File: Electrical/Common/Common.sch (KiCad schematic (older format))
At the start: 76 parts, among them J201 01x03, J202 01x04, J203 01x03, J204 01x04, J205 01x03, J206 USB_OTG, J207 01x04, J208 01x02, J209 01x04, J210 01x02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

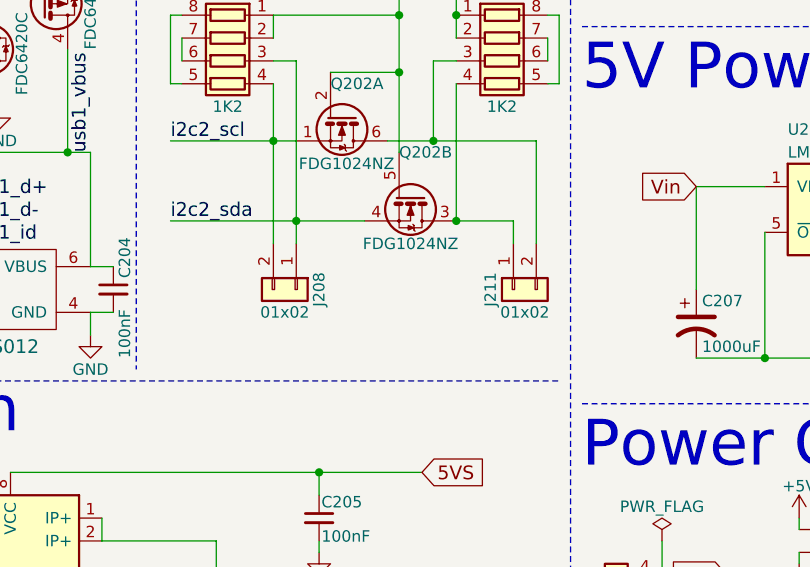
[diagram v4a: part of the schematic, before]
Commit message: Made pin one consistantly SCL on both sets of I2C headers.
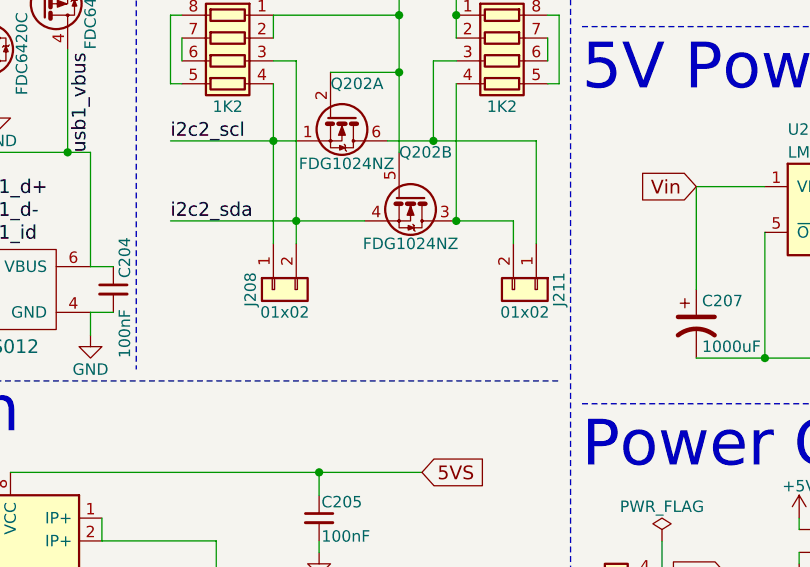
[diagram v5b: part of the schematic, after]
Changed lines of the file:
@@
 LIBS:allegro
 LIBS:mechanical
-LIBS:Dual-cache
+LIBS:Quad-cache
 EELAYER 25 0
 EELAYER END
 $Descr A4 11693 8268
 encoding utf-8
-Sheet 2 4
+Sheet 2 6
 Title ""
 Date ""
@@
 L Conn_01x02 J208
 U 1 1 5A50A269
-P 6200 3250
-F 0 "J208" H 6200 3350 50  0000 C CNN
-F 1 "01x02" V 6300 3200 50  0000 C CNN
-F 2 "Pin_Headers:Pin_Header_Straight_1x02_Pitch2.54mm" H 6200 3250 50  0001 C CNN
-F 3 "" H 6200 3250 50  0001 C CNN
-	1    6200 3250
-	0    1    1    0
+P 6100 3250
+F 0 "J208" H 6100 3350 50  0000 C CNN
+F 1 "01x02" V 6200 3200 50  0000 C CNN
+F 2 "Pin_Headers:Pin_Header_Straight_1x02_Pitch2.54mm" H 6100 3250 50  0001 C CNN
+F 3 "" H 6100 3250 50  0001 C CNN
+	1    6100 3250
+	0    -1   1    0
 $EndComp
 $Comp
@@
 L Conn_01x02 J211
 U 1 1 5A5787B1
-P 7150 3250
-F 0 "J211" H 7150 3350 50  0000 C CNN
-F 1 "01x02" V 7250 3200 50  0000 C CNN
-F 2 "Pin_Headers:Pin_Header_Straight_1x02_Pitch2.54mm" H 7150 3250 50  0001 C CNN
-F 3 "" H 7150 3250 50  0001 C CNN
-	1    7150 3250
-	0    -1   1    0
-$EndComp
-$Comp
+P 7250 3250
+F 0 "J211" H 7250 3350 50  0000 C CNN
+F 1 "01x02" V 7350 3200 50  0000 C CNN
+F 2 "Pin_Headers:Pin_Header_Straight_1x02_Pitch2.54mm" H 7250 3250 50  0001 C CNN
+F 3 "" H 7250 3250 50  0001 C CNN
+	1    7250 3250
+	0    1    1    0
+$EndComp
+$Comp

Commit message: Used bigger capacitor footprints to allow for 1000 uF electrolytics at 50V
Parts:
- C207, C208: footprint Capacitors_SMD:CP_Elec_8x10 -> footprints:CP_Elec_17x17
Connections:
- wire segments 290 -> 289

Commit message: ACS712 -> ACS723
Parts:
- removed U202, U203: ACS712ELCTR-05B-T, Housings_SOIC:SOIC-8_3.9x4.9mm_Pitch1.27mm, symbol ACS712ELCTR-05B-T
- added U202, U203: ACS723LLCTR-05AB-T, Housings_SOIC:SOIC-8_3.9x4.9mm_Pitch1.27mm, symbol ACS722LLCTR-05AB-T
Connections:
- no-connect marks 4 -> 6
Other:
- moved on the sheet: C201, C202, RN201
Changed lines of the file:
@@
 LIBS:allegro
 LIBS:mechanical
-LIBS:Quad-cache
+LIBS:Dual-cache
 EELAYER 25 0
 EELAYER END
 $Descr A4 11693 8268
 encoding utf-8
-Sheet 2 6
+Sheet 2 4
 Title ""
 Date ""
@@
 IP_5V
 $Comp
-L ACS712ELCTR-05B-T U202
-U 1 1 5A56E5BD
-P 4950 4450
-F 0 "U202" H 5050 4900 50  0000 L CNN
-F 1 "ACS712ELCTR-05B-T" H 5050 4800 50  0000 L CNN
-F 2 "Housings_SOIC:SOIC-8_3.9x4.9mm_Pitch1.27mm" H 5050 4100 50  0001 L CIN
-F 3 "" H 4950 4450 50  0001 C CNN
-	1    4950 4450
-	-1   0    0    -1
-$EndComp
-$Comp
-L ACS712ELCTR-05B-T U203
-U 1 1 5A56F4CA
-P 5400 5400
-F 0 "U203" H 5600 5750 50  0000 L CNN
-F 1 "ACS712ELCTR-05B-T" H 4250 5150 50  0000 L CNN
-F 2 "Housings_SOIC:SOIC-8_3.9x4.9mm_Pitch1.27mm" H 5500 5050 50  0001 L CIN
-F 3 "" H 5400 5400 50  0001 C CNN
-	1    5400 5400
-	-1   0    0    -1
-$EndComp
-$Comp
 L Conn_01x04 JP201
 U 1 1 5A5701C7
@@
 L C_Small C201
 U 1 1 5A576DFD
-P 4550 4800
-F 0 "C201" H 4650 4800 50  0000 L CNN
-F 1 "1nF" H 4400 4850 50  0000 L CNN
-F 2 "Capacitors_SMD:C_0603_HandSoldering" H 4550 4800 50  0001 C CNN
-F 3 "" H 4550 4800 50  0001 C CNN
-	1    4550 4800
-	1    0    0    -1
+P 4550 4900
+F 0 "C201" V 4600 4650 50  0000 L CNN
+F 1 "1nF" V 4450 4800 50  0000 L CNN
+F 2 "Capacitors_SMD:C_0603_HandSoldering" H 4550 4900 50  0001 C CNN
+F 3 "" H 4550 4900 50  0001 C CNN
+	1    4550 4900
+	0    -1   -1   0
 $EndComp
 $Comp
 L C_Small C202
 U 1 1 5A57755C
-P 5000 5750
-F 0 "C202" H 5100 5750 50  0000 L CNN
-F 1 "1nF" H 4850 5800 50  0000 L CNN
-F 2 "Capacitors_SMD:C_0603_HandSoldering" H 5000 5750 50  0001 C CNN
-F 3 "" H 5000 5750 50  0001 C CNN
-	1    5000 5750
-	1    0    0    -1
-$EndComp
-Text Label 3950 4800 1    60   ~ 0
+P 4700 5750
+F 0 "C202" H 4450 5650 50  0000 L CNN
+F 1 "1nF" H 4550 5800 50  0000 L CNN
+F 2 "Capacitors_SMD:C_0603_HandSoldering" H 4700 5750 50  0001 C CNN
+F 3 "" H 4700 5750 50  0001 C CNN
+	1    4700 5750
+	1    0    0    -1
+$EndComp
+Text Label 3950 4950 1    60   ~ 0
 ain4
-Text Label 3950 4900 3    60   ~ 0
+Text Label 3950 5050 3    60   ~ 0
 ain7
 NoConn ~ 2800 2900
@@
 L R_Pack04 RN201
 U 1 1 5A58826C
-P 4150 5000
-F 0 "RN201" V 3850 5000 50  0000 C CNN
-F 1 "1K2" V 4350 5000 50  0000 C CNN
-F 2 "footprints:R_Array_1206x04" V 4425 5000 50  0001 C CNN
-F 3 "" H 4150 5000 50  0001 C CNN
-	1    4150 5000
+P 4150 5150
+F 0 "RN201" V 3850 5150 50  0000 C CNN
+F 1 "1K2" V 4350 5150 50  0000 C CNN
+F 2 "footprints:R_Array_1206x04" V 4425 5150 50  0001 C CNN
+F 3 "" H 4150 5150 50  0001 C CNN
+	1    4150 5150
 	0    1    1    0
 $EndComp
@@
 L GND #PWR018
 U 1 1 5A589958
-P 4350 5200
-F 0 "#PWR018" H 4350 4950 50  0001 C CNN
-F 1 "GND" H 4350 5050 50  0000 C CNN
-F 2 "" H 4350 5200 50  0001 C CNN
-F 3 "" H 4350 5200 50  0001 C CNN
-	1    4350 5200
+P 4350 5350
+F 0 "#PWR018" H 4350 5100 50  0001 C CNN
+F 1 "GND" H 4350 5200 50  0000 C CNN
+F 2 "" H 4350 5350 50  0001 C CNN
+F 3 "" H 4350 5350 50  0001 C CNN
+	1    4350 5350
 	1    0    0    -1
 $EndComp
@@
 Wire Wire Line
 	6700 4750 6750 4750
-Connection ~ 4350 5100
+Connection ~ 4350 5250
 Wire Wire Line
 	3200 1550 3200 1700
@@
 	9150 5000 9150 4950
 Wire Wire Line
-	7000 5000 6500 5000
+	6500 5000 7000 5000
 Wire Wire Line
 	6700 5000 6700 4750
 Wire Wire Line
-	3850 5100 3950 5100
-Wire Wire Line
-	3850 4800 3850 5100
-Wire Wire Line
-	3950 4800 3850 4800
-Wire Wire Line
-	3950 5000 3950 4900
-Wire Wire Line
-	4450 4900 4350 4900
+	3850 5250 3950 5250
+Wire Wire Line
+	3850 4950 3850 5250
+Wire Wire Line
+	3950 4950 3850 4950
+Wire Wire Line
+	3950 5150 3950 5050
+Wire Wire Line
+	4450 5050 4350 5050
 Connection ~ 8350 6300
 Wire Wire Line
@@
 	8200 6300 8200 6200
 Wire Wire Line
-	8850 6300 8200 6300
+	8200 6300 8850 6300
 Connection ~ 8350 5900
 Wire Wire Line
-	8850 5900 8850 6300
-Wire Wire Line
-	8200 5900 8850 5900
-Wire Wire Line
-	8200 5800 8200 5900
-Wire Wire Line
-	7800 5800 8200 5800
+	8850 6300 8850 5900
+Wire Wire Line
+	8850 5900 8200 5900
+Wire Wire Line
+	8200 5900 8200 5800
+Wire Wire Line
+	8200 5800 7800 5800
 Connection ~ 4550 2650
 Connection ~ 6950 5300
@@
 Connection ~ 6650 2300
 Wire Wire Line
-	6350 2300 6650 2300
+	6650 2300 6350 2300
 Wire Wire Line
 	6650 1700 6650 2650
@@
 	6200 950  7050 950
 Wire Wire Line
-	4350 5000 4350 5200
+	4350 5150 4350 5350
 Wire Wire Line
 	4450 5200 5000 5200
 Wire Wire Line
-	4450 4900 4450 5200
-Wire Wire Line
-	4350 4250 4550 4250
-Wire Wire Line
-	4350 4800 4350 4250
-Wire Wire Line
-	5400 5850 5000 5850
-Wire Wire Line
-	4550 4900 5000 4900
+	4450 5050 4450 5200
+Wire Wire Line
+	4350 4250 4350 4950
+Wire Wire Line
+	5400 5850 4700 5850
 Connection ~ 4900 7500
 Connection ~ 4900 7400
@@
 	2900 7300 3000 7300
 Wire Wire Line
-	5000 5650 5000 5500
-Wire Wire Line
-	4550 4700 4550 4550
+	4700 5200 4700 5650
 Connection ~ 4950 4900
 Wire Wire Line
@@
 Connection ~ 8750 3550
 Wire Wire Line
-	8750 3200 8750 3550
+	8750 3550 8750 3200
 Wire Wire Line
 	9750 3250 9750 3000
@@
 Connection ~ 2850 3650
 Wire Wire Line
-	2800 3650 2850 3650
+	2850 3650 2800 3650
 Connection ~ 2850 3600
 Wire Wire Line
-	2800 3600 2850 3600
+	2850 3600 2800 3600
 Connection ~ 2850 3550
 Wire Wire Line
@@
 Wire Wire Line
 	9650 6400 10150 6400
+$Comp
+L ACS722LLCTR-05AB-T U203
+U 1 1 5A7DF043
+P 5400 5400
+F 0 "U203" H 5500 5750 50  0000 L CNN
+F 1 "ACS723LLCTR-05AB-T" H 4450 5050 50  0000 L CNN
+F 2 "Housings_SOIC:SOIC-8_3.9x4.9mm_Pitch1.27mm" H 5500 5050 50  0001 L CIN
+F 3 "" H 5400 5400 50  0001 C CNN
+	1    5400 5400
+	-1   0    0    -1
+$EndComp
+Connection ~ 4700 5200
+$Comp
+L ACS722LLCTR-05AB-T U202
+U 1 1 5A7E0560
+P 4950 4450
+F 0 "U202" H 5050 4900 50  0000 L CNN
+F 1 "ACS723LLCTR-05AB-T" H 5050 4800 50  0000 L CNN
+F 2 "Housings_SOIC:SOIC-8_3.9x4.9mm_Pitch1.27mm" H 5050 4100 50  0001 L CIN
+F 3 "" H 4950 4450 50  0001 C CNN
+	1    4950 4450
+	-1   0    0    -1
+$EndComp
+Connection ~ 4350 4900
+Wire Wire Line
+	4450 4900 4350 4900
+Wire Wire Line
+	4550 4250 4350 4250
+Wire Wire Line
+	5000 4900 4650 4900
+NoConn ~ 4550 4550
+NoConn ~ 5000 5500
 $EndSCHEMATC

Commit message: FB <> Fuse; FB == Ferrite Bead
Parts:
- removed F201, F202: Fuse, SMD_Packages:SMD-1206_Pol, symbol Fuse_Small
- added FB201, FB202: 120, SMD_Packages:SMD-1206_Pol, symbol Ferrite_Bead_Small
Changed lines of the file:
@@
 LIBS:allegro
 LIBS:mechanical
-LIBS:Dual-cache
+LIBS:Quad-cache
 EELAYER 25 0
 EELAYER END
 $Descr A4 11693 8268
 encoding utf-8
-Sheet 2 4
+Sheet 2 6
 Title ""
 Date ""
@@
 Text Label 1300 3250 2    30   ~ 0
 usb1_drvvbus
-$Comp
-L Fuse_Small F202
-U 1 1 5A58792D
-P 4650 2650
-F 0 "F202" H 4650 2590 50  0000 C CNN
-F 1 "Fuse" H 4650 2710 50  0000 C CNN
-F 2 "SMD_Packages:SMD-1206_Pol" H 4650 2650 50  0001 C CNN
-F 3 "" H 4650 2650 50  0001 C CNN
-	1    4650 2650
-	1    0    0    -1
-$EndComp
-$Comp
-L Fuse_Small F201
-U 1 1 5A5884F0
-P 4050 3450
-F 0 "F201" H 4050 3390 50  0000 C CNN
-F 1 "Fuse" H 4050 3510 50  0000 C CNN
-F 2 "SMD_Packages:SMD-1206_Pol" H 4050 3450 50  0001 C CNN
-F 3 "" H 4050 3450 50  0001 C CNN
-	1    4050 3450
-	1    0    0    -1
-$EndComp
 Text Label 4750 2950 0    60   ~ 0
 usb1_d-
@@
 L PWR_FLAG #FLG030
 U 1 1 5A592059
-P 4550 2650
-F 0 "#FLG030" H 4550 2725 50  0001 C CNN
-F 1 "PWR_FLAG" H 4550 2800 50  0000 C CNN
-F 2 "" H 4550 2650 50  0001 C CNN
-F 3 "" H 4550 2650 50  0001 C CNN
-	1    4550 2650
+P 4500 2650
+F 0 "#FLG030" H 4500 2725 50  0001 C CNN
+F 1 "PWR_FLAG" H 4500 2800 50  0000 C CNN
+F 2 "" H 4500 2650 50  0001 C CNN
+F 3 "" H 4500 2650 50  0001 C CNN
+	1    4500 2650
 	1    0    0    1
 $EndComp
@@
 Text Label 10150 4850 2    60   ~ 0
 usb1_5V
-Text Label 4550 2650 1    60   ~ 0
+Text Label 4500 2650 1    60   ~ 0
 usb1_5V
 Text Label 5300 2650 1    60   ~ 0
@@
 Wire Wire Line
 	8200 5800 7800 5800
-Connection ~ 4550 2650
+Connection ~ 4500 2650
 Connection ~ 6950 5300
 Connection ~ 6700 5000
@@
 	3950 3250 3950 3450
 Wire Wire Line
-	4750 2650 5300 2650
-Wire Wire Line
-	4350 2650 4550 2650
+	4800 2650 5300 2650
+Wire Wire Line
+	4350 2650 4600 2650
 Wire Wire Line
 	2800 2150 2800 2250
@@
 	4550 4250 4350 4250
 Wire Wire Line
-	5000 4900 4650 4900
+	4650 4900 5000 4900
 NoConn ~ 4550 4550
 NoConn ~ 5000 5500
+$Comp
+L Ferrite_Bead_Small FB202
+U 1 1 5A7E3264
+P 4700 2650
+F 0 "FB202" H 4775 2700 50  0000 L CNN
+F 1 "120" H 4775 2600 50  0000 L CNN
+F 2 "SMD_Packages:SMD-1206_Pol" V 4630 2650 50  0001 C CNN
+F 3 "" H 4700 2650 50  0001 C CNN
+	1    4700 2650
+	0    -1   -1   0
+$EndComp
+$Comp
+L Ferrite_Bead_Small FB201
+U 1 1 5A7E3ED4
+P 4050 3450
+F 0 "FB201" V 4000 3550 50  0000 L CNN
+F 1 "120" V 3900 3450 50  0000 L CNN
+F 2 "SMD_Packages:SMD-1206_Pol" V 3980 3450 50  0001 C CNN
+F 3 "" H 4050 3450 50  0001 C CNN
+	1    4050 3450
+	0    -1   -1   0
+$EndComp
 $EndSCHEMATC
